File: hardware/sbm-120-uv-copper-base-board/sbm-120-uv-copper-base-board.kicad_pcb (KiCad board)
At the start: 2 copper layers, 16.1 x 21.2 mm, 5 parts, among them J1 +, J2 THERMISTOR, J3 -, U1 SBM-120-UV

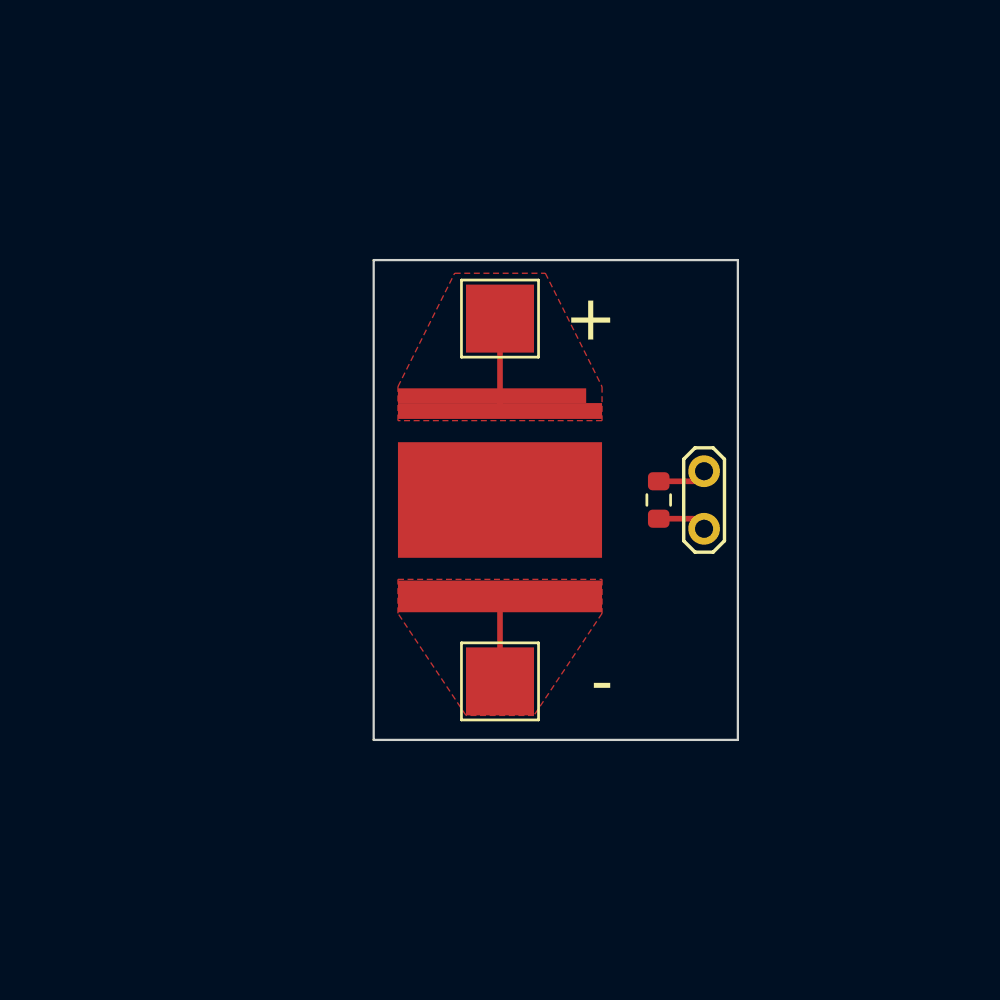
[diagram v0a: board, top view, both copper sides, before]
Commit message: single led copper base + uven pocket finished
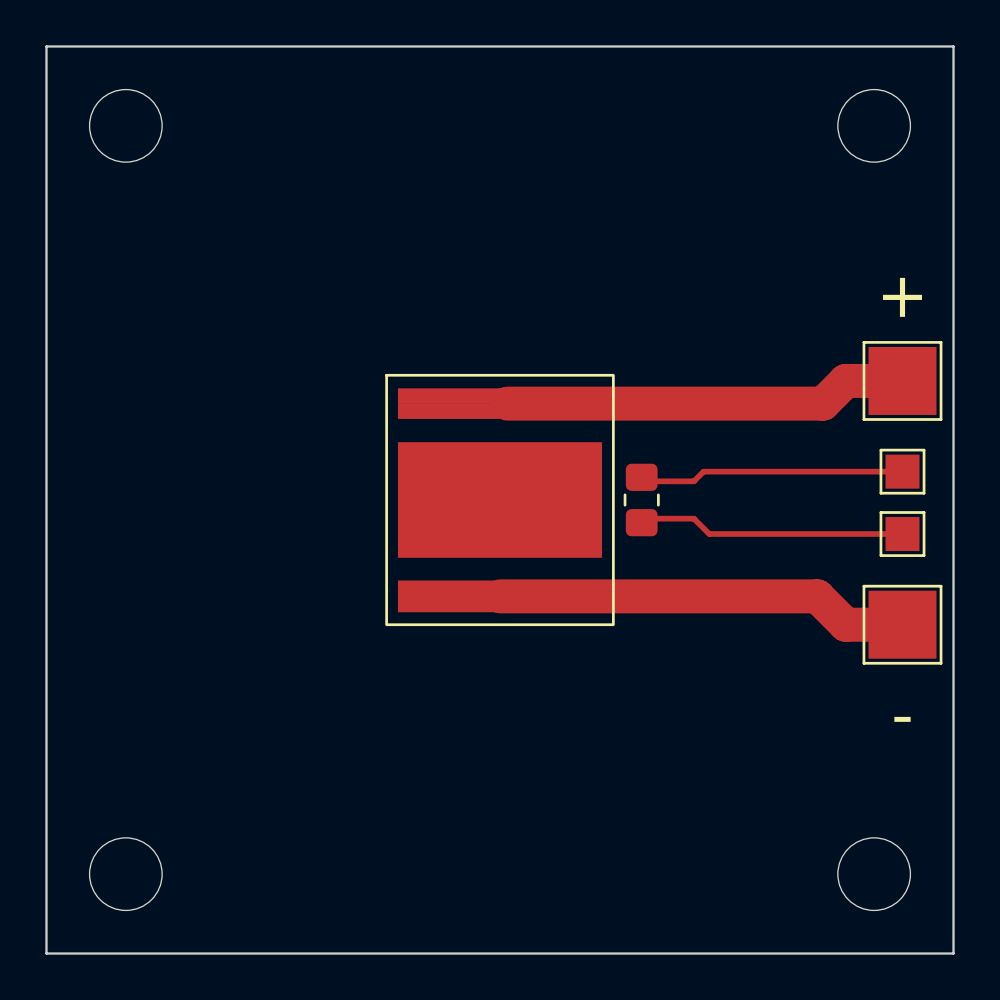
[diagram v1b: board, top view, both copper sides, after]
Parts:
- added H1: MountingHole, MountingHole:MountingHole_3.2mm_M3, F.Cu at (153.4, 94.8)
- added H2: MountingHole, MountingHole:MountingHole_3.2mm_M3, F.Cu at (120.4, 61.8)
- added H3: MountingHole, MountingHole:MountingHole_3.2mm_M3, F.Cu at (153.4, 61.8)
- added H4: MountingHole, MountingHole:MountingHole_3.2mm_M3, F.Cu at (120.4, 94.8)
- added J4: temp-, TestPoint:TestPoint_Pad_1.5x1.5mm, F.Cu at (154.7, 79.8)
- J2: value THERMISTOR -> temp+; footprint TestPoint:TestPoint_2Pads_Pitch2.54mm_Drill0.8mm -> TestPoint:TestPoint_Pad_1.5x1.5mm
- TH1: footprint Resistor_SMD:R_0603_1608Metric -> Resistor_SMD:R_0805_2012Metric_Pad1.20x1.40mm_HandSolder
- moved J1 18.0 mm to (154.7, 73.1)
- moved J3 17.9 mm to (154.7, 83.8)
- moved J2 8.75 mm to (154.7, 77.1), turned to 0 degrees
- moved TH1 0.75 mm to (143.2, 78.3)
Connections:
- TH1 pad 1: Net-(J2-Pad2) -> Net-(TH1-Pad1)
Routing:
- net Net-(J3-Pad1): track 3.75 -> 18.3 mm
- net Net-(J1-Pad1): track 4.08 -> 17.8 mm
- net Net-(TH1-Pad1): track 0.00 -> 11.9 mm
- net Net-(TH1-Pad2): track 2.18 -> 11.7 mm
- net Net-(J2-Pad2): track 2.18 -> 0.00 mm
- removed copper zone on F.Cu, net (none)
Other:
- board size 16.1 x 21.2 mm -> 40 x 40 mm
- board text added: "DH"
